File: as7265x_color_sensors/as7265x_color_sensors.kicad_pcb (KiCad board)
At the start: 2 copper layers, 37 parts, among them J1 Conn_01x06_Male, J2 RJ12, J3 RJ12, U1 AS72652, U2 AS72653, U3 AS72651, U4 AT25SF041

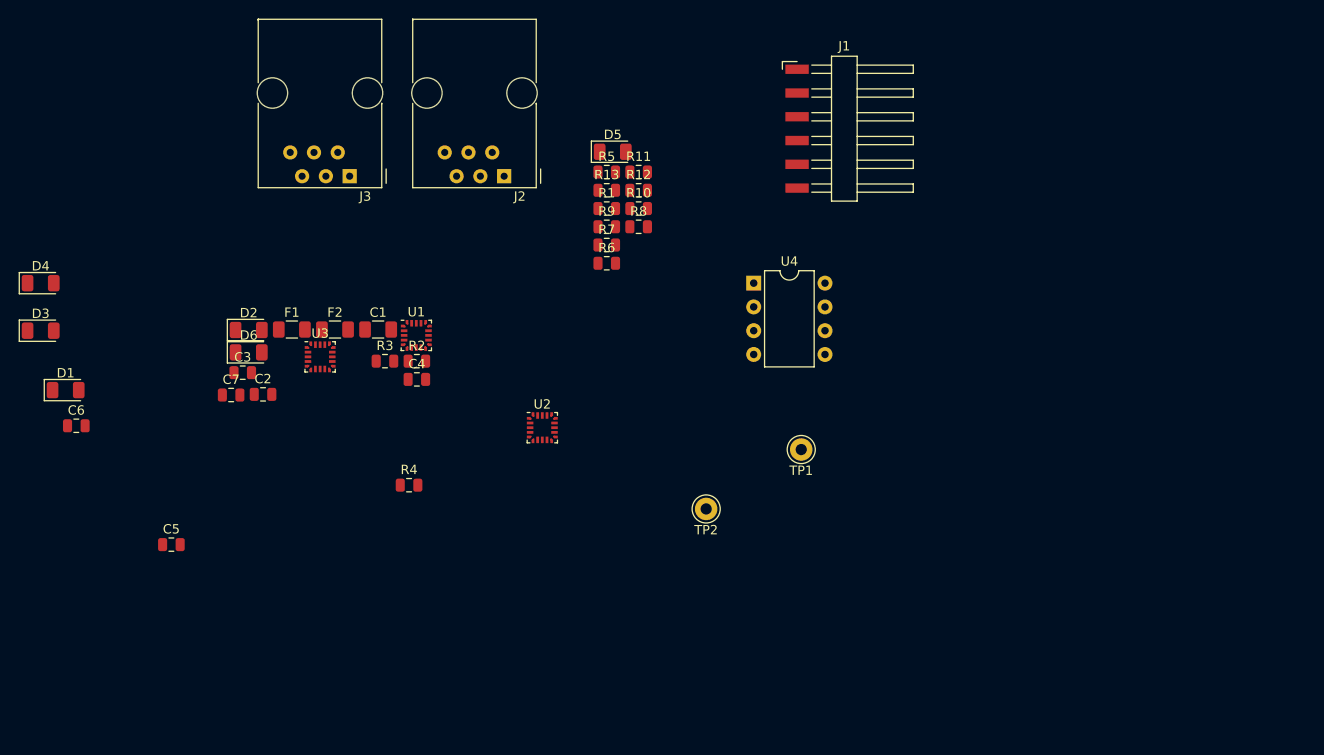
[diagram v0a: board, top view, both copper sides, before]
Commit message: chip footprints fixed, started layout
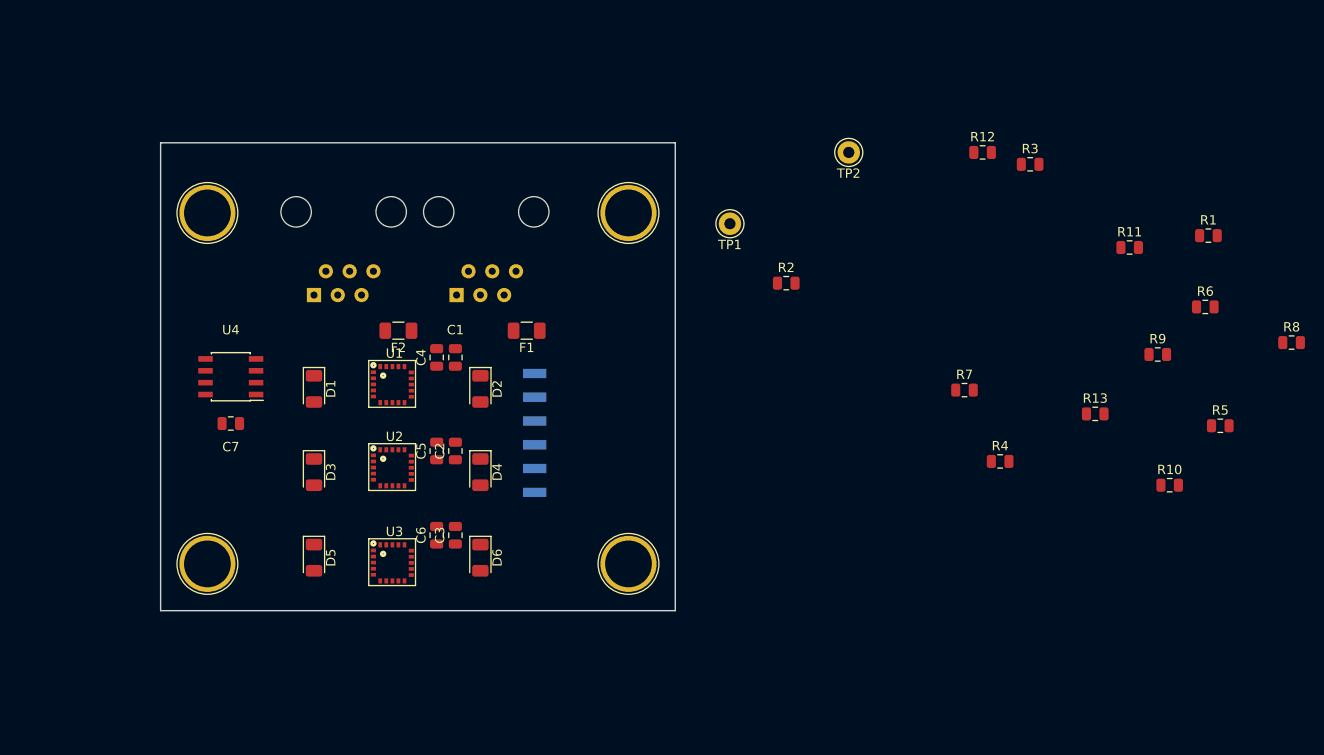
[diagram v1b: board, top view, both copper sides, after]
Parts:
- added REF**: TestPoint_Plated_Hole_D5.0mm, TestPoint:TestPoint_Plated_Hole_D5.0mm, F.Cu at (33.1, 40.8)
- added REF**: TestPoint_Plated_Hole_D5.0mm, TestPoint:TestPoint_Plated_Hole_D5.0mm, F.Cu at (78.1, 40.8)
- added REF**: TestPoint_Plated_Hole_D5.0mm, TestPoint:TestPoint_Plated_Hole_D5.0mm, F.Cu at (78.1, 78.3)
- added REF**: TestPoint_Plated_Hole_D5.0mm, TestPoint:TestPoint_Plated_Hole_D5.0mm, F.Cu at (33.1, 78.3)
- C1: footprint Capacitor_SMD:C_1206_3216Metric -> Capacitor_SMD:C_0805_2012Metric
- J1, J2, J3: moved to B.Cu
- U1: value AS72652 -> AS72651; footprint Package_DFN_QFN:ST_UFQFPN-20_3x3mm_P0.5mm -> MRV_SMD_Packages:LGA-20_4.5mm_4.7mm_2.5mm
- U2: value AS72653 -> AS72652; footprint Package_DFN_QFN:ST_UFQFPN-20_3x3mm_P0.5mm -> MRV_SMD_Packages:LGA-20_4.5mm_4.7mm_2.5mm
- U3: value AS72651 -> AS72653; footprint Package_DFN_QFN:ST_UFQFPN-20_3x3mm_P0.5mm -> MRV_SMD_Packages:LGA-20_4.5mm_4.7mm_2.5mm
- U4: footprint Package_DIP:DIP-8_W7.62mm -> Package_SO:SOIC-8_3.9x4.9mm_P1.27mm
- moved R3 72.1 mm to (121.0, 35.6)
- moved R5 71.0 mm to (141.3, 63.5)
- moved R8 70.9 mm to (148.9, 54.6)
- moved R1 64.4 mm to (140.0, 43.2)
- moved R6 64.1 mm to (139.7, 50.8)
- moved R10 64.0 mm to (135.9, 69.8)
- moved R4 63.2 mm to (117.8, 67.3)
- moved R9 60.4 mm to (134.6, 55.9)
- moved R13 57.4 mm to (127.9, 62.2)
- moved U4 56.8 mm to (35.6, 58.3), turned to 180 degrees
- moved D5 53.9 mm to (44.5, 77.6), turned to 270 degrees
- moved R11 53.1 mm to (131.6, 44.5)
- moved D4 51.1 mm to (62.2, 68.5), turned to 270 degrees
- moved J1 42.9 mm to (73.6, 64.3)
- moved R7 41.3 mm to (114.0, 59.7)
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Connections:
- U1 pad 11: Net-(U1-Pad11) -> /RXI
- U1 pad 12: Net-(U1-Pad12) -> /TXO
- U1 pad 13: Net-(U1-Pad13) -> /~INT
- U1 pad 15: /LED4 -> /LED2
- U1 pad 18: /LED3 -> /LED1
- U1 pad 5: Net-(R11-Pad2) -> Net-(U1-Pad5)
- U1 pad 7: Net-(R13-Pad2) -> Net-(U1-Pad7)
- U1 pad 8: Net-(U1-Pad8) -> Net-(R8-Pad1)
- U2 pad 15: /LED6 -> /LED4
- U2 pad 18: /LED5 -> /LED3
- U2 pad 5: Net-(R10-Pad2) -> Net-(R11-Pad2)
- U2 pad 7: Net-(R12-Pad2) -> Net-(R13-Pad2)
- U3 pad 11: /RXI -> Net-(U3-Pad11)
- U3 pad 12: /TXO -> Net-(U3-Pad12)
- U3 pad 13: /~INT -> Net-(U3-Pad13)
- U3 pad 15: /LED2 -> /LED6
- U3 pad 18: /LED1 -> /LED5
- U3 pad 5: Net-(U3-Pad5) -> Net-(R10-Pad2)
- U3 pad 7: Net-(U3-Pad7) -> Net-(R12-Pad2)
- U3 pad 8: Net-(R8-Pad1) -> Net-(U3-Pad8)
- U4 pad 1: Net-(U3-Pad6) -> Net-(U1-Pad6)
- U4 pad 2: Net-(U3-Pad5) -> Net-(U1-Pad5)
- U4 pad 5: Net-(U3-Pad4) -> Net-(U1-Pad4)
- U4 pad 6: Net-(U3-Pad3) -> Net-(U1-Pad3)
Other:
- board outline added: 55 x 50 mm

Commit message: adding TVS diode arrays
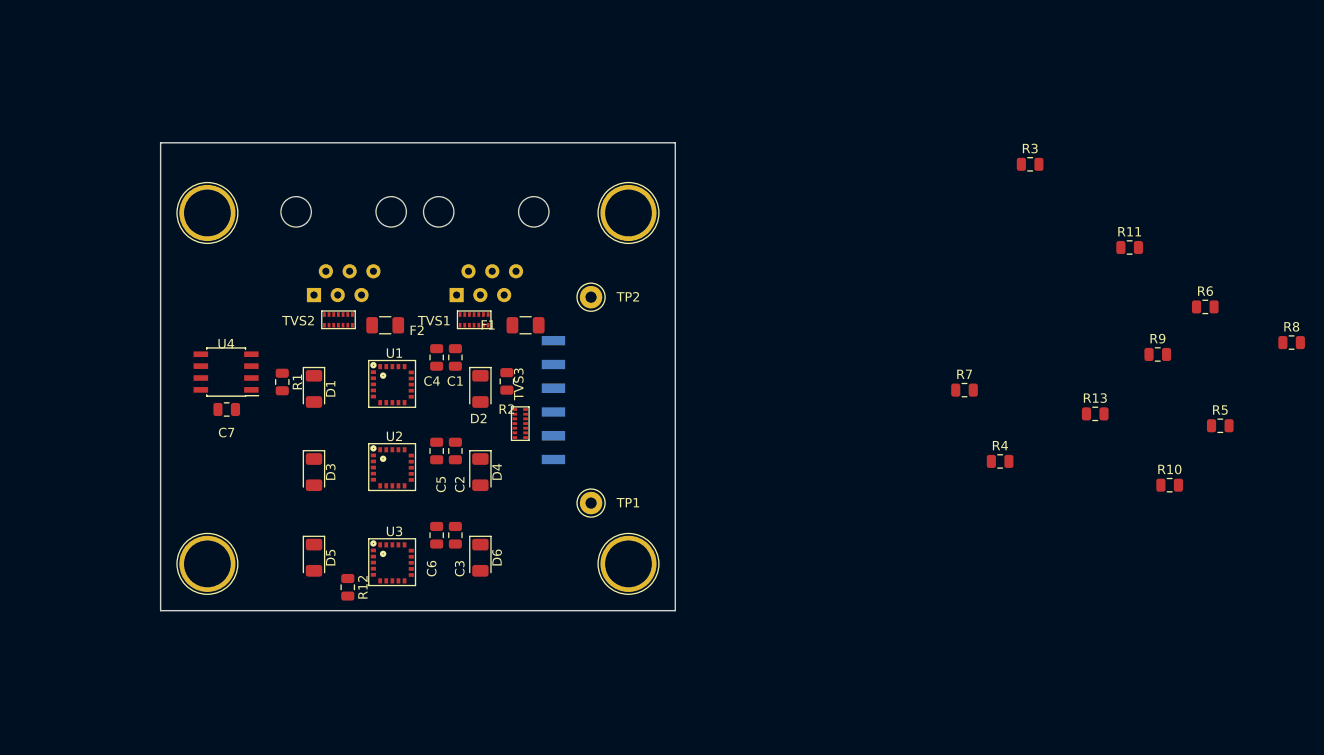
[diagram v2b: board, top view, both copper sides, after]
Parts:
- added TVS1: SP3012-06UTG, MRV_SMD_Packages:uDFN-14_3.5x1.35x0.5mm, F.Cu at (60.1, 52.8)
- added TVS2: SP3012-06UTG, MRV_SMD_Packages:uDFN-14_3.5x1.35x0.5mm, F.Cu at (45.6, 52.8)
- added TVS3: SP3012-06UTG, MRV_SMD_Packages:uDFN-14_3.5x1.35x0.5mm, F.Cu at (65.9, 61.8)
- moved R1 100.2 mm to (41.1, 58.8), turned to 270 degrees
- moved R12 82.2 mm to (48.1, 80.8), turned to 270 degrees
- moved TP1 33.3 mm to (74.1, 71.8)
- moved R2 31.6 mm to (65.1, 58.8), turned to 90 degrees
- moved TP2 31.6 mm to (74.1, 49.8)
- moved J1 4.03 mm to (75.6, 60.8)
- moved C7 1.56 mm to (35.1, 61.8)
- moved F2 1.52 mm to (52.1, 52.8), turned to 0 degrees
- moved U4 0.71 mm to (35.1, 57.8)
- moved F1 0.59 mm to (67.1, 52.8)

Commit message: added test points, more layout progress
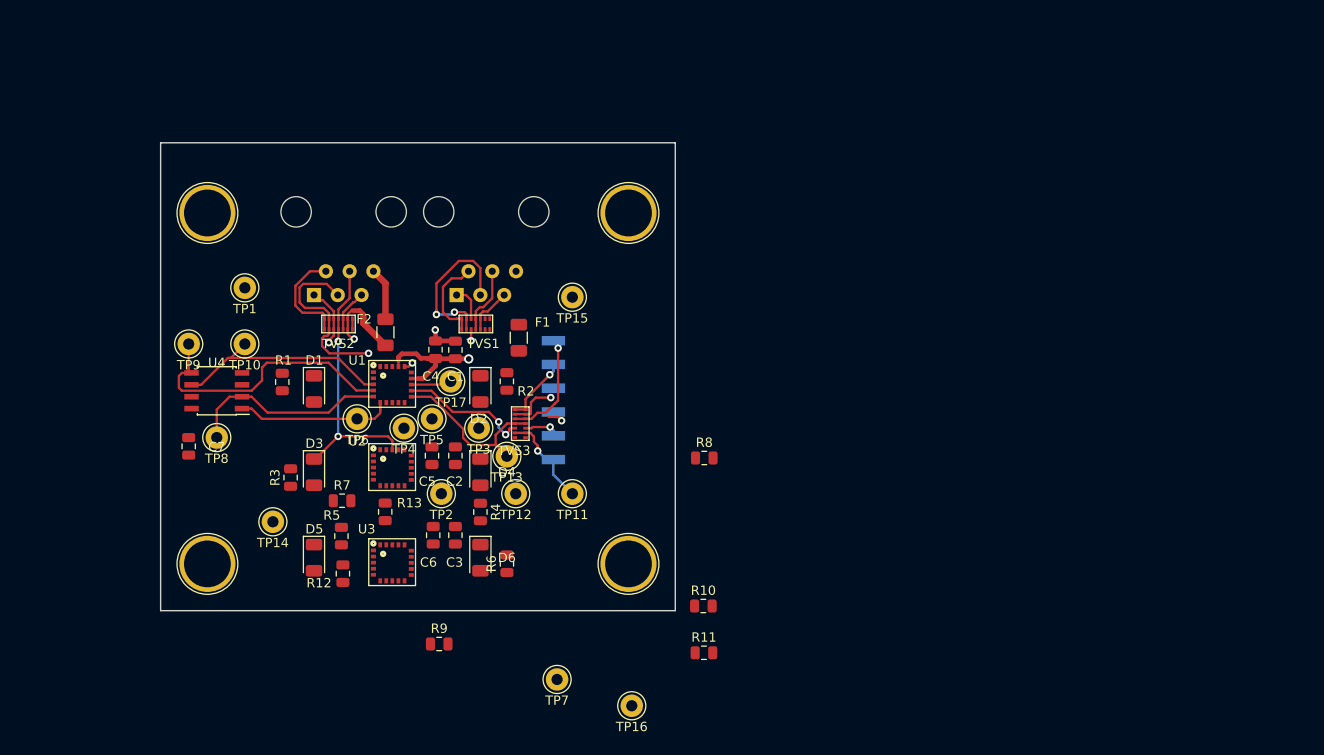
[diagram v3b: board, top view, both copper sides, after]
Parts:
- added TP10: TestPoint, Connector_Pin:Pin_D1.0mm_L10.0mm_LooseFit, F.Cu at (37.1, 54.8)
- added TP11: TestPoint, Connector_Pin:Pin_D1.0mm_L10.0mm_LooseFit, F.Cu at (72.1, 70.8)
- added TP12: TestPoint, Connector_Pin:Pin_D1.0mm_L10.0mm_LooseFit, F.Cu at (66.0, 70.8)
- added TP13: TestPoint, Connector_Pin:Pin_D1.0mm_L10.0mm_LooseFit, F.Cu at (65.1, 66.8)
- added TP14: TestPoint, Connector_Pin:Pin_D1.0mm_L10.0mm_LooseFit, F.Cu at (40.1, 73.8)
- added TP15: TestPoint, Connector_Pin:Pin_D1.0mm_L10.0mm_LooseFit, F.Cu at (72.1, 49.8)
- added TP16: TestPoint, Connector_Pin:Pin_D1.0mm_L10.0mm_LooseFit, F.Cu at (78.4, 93.4)
- added TP17: TestPoint, Connector_Pin:Pin_D1.0mm_L10.0mm_LooseFit, F.Cu at (59.1, 58.8)
- added TP3: TestPoint, Connector_Pin:Pin_D1.0mm_L10.0mm_LooseFit, F.Cu at (62.1, 63.8)
- added TP4: TestPoint, Connector_Pin:Pin_D1.0mm_L10.0mm_LooseFit, F.Cu at (54.1, 63.8)
- added TP5: TestPoint, Connector_Pin:Pin_D1.0mm_L10.0mm_LooseFit, F.Cu at (57.1, 62.8)
- added TP6: TestPoint, Connector_Pin:Pin_D1.0mm_L10.0mm_LooseFit, F.Cu at (49.1, 62.8)
- added TP7: TestPoint, Connector_Pin:Pin_D1.0mm_L10.0mm_LooseFit, F.Cu at (70.4, 90.6)
- added TP8: TestPoint, Connector_Pin:Pin_D1.0mm_L10.0mm_LooseFit, F.Cu at (34.1, 64.8)
- added TP9: TestPoint, Connector_Pin:Pin_D1.0mm_L10.0mm_LooseFit, F.Cu at (31.1, 54.8)
- moved R5 94.7 mm to (47.4, 75.3), turned to 90 degrees
- moved R3 85.8 mm to (42.0, 69.0), turned to 90 degrees
- moved R9 82.8 mm to (57.8, 86.8)
- moved R6 79.5 mm to (65.1, 78.2), turned to 90 degrees
- moved R13 76.6 mm to (52.1, 72.7), turned to 90 degrees
- moved R7 67.6 mm to (47.5, 71.5)
- moved R8 64.0 mm to (86.2, 66.9)
- moved R11 62.8 mm to (86.1, 87.8)
- moved R4 55.8 mm to (62.2, 72.7), turned to 270 degrees
- moved R10 51.5 mm to (86.1, 82.8)
- moved TP1 43.6 mm to (37.1, 48.8)
- moved TP2 26.4 mm to (58.1, 70.8)
- moved C7 5.66 mm to (31.1, 65.7), turned to 270 degrees
- moved U4 2.24 mm to (34.1, 59.8)
- moved R12 1.54 mm to (47.5, 79.3)
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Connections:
- TP1 pad 1: /DTR -> +3V3
- TP2 pad 1: /CTS -> Net-(TP2-Pad1)
- U1 pad 10: Net-(U1-Pad10) -> Net-(TP2-Pad1)
- U2 pad 10: Net-(U1-Pad10) -> Net-(TP2-Pad1)
- U3 pad 10: Net-(U1-Pad10) -> Net-(TP2-Pad1)
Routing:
- net Net-(TP9-Pad1): track 0.00 -> 30.1 mm
- net /LED3: track 0.00 -> 28.7 mm, vias 0 -> 2
- net /RXI: track 0.00 -> 28.3 mm, vias 0 -> 1
- net GND: track 0.00 -> 27.7 mm, vias 0 -> 5
- net +3V3: track 0.00 -> 27.4 mm, vias 0 -> 3
- net Net-(TP10-Pad1): track 0.00 -> 24.2 mm
- net /TXO: track 0.00 -> 22.5 mm, vias 0 -> 3
- net Net-(TP8-Pad1): track 0.00 -> 21.7 mm
- net /LED2: track 0.00 -> 19.2 mm, vias 0 -> 1
- net /LED6: track 0.00 -> 17.4 mm, vias 0 -> 2
- net Net-(TP6-Pad1): track 0.00 -> 17.1 mm
- net /LED1: track 0.00 -> 11.2 mm
- net /DTR: track 0.00 -> 10.5 mm, vias 0 -> 1
- net /LED5: track 0.00 -> 9.58 mm
- net /CTS: track 0.00 -> 7.19 mm, vias 0 -> 1
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
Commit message: worked on layout
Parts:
- R8, R9: moved to B.Cu
- moved R11 44.1 mm to (46.8, 67.8), turned to 90 degrees
- moved R10 36.9 mm to (49.3, 79.2), turned to 90 degrees
- moved R8 30.9 mm to (56.4, 58.8), turned to 90 degrees
- moved R9 28.4 mm to (62.0, 58.8), turned to 270 degrees
- moved TP7 13.1 mm to (57.7, 87.6)
- moved TP16 7.69 mm to (73.0, 88.0)
- moved C5 1.63 mm to (58.3, 65.7), turned to 0 degrees
- moved C2 1.62 mm to (58.3, 67.8), turned to 0 degrees
- moved TP4 1.50 mm to (52.6, 63.5)
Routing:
- net /LED5: track 9.58 -> 76.3 mm, vias 0 -> 3
- net /LED6: track 17.4 -> 73.6 mm, vias 2 -> 4
- net Net-(TP3-Pad1): track 0.00 -> 55.4 mm, vias 0 -> 3
- net +3V3: track 27.4 -> 79.6 mm, vias 3 -> 17
- net Net-(TP2-Pad1): track 0.00 -> 30.9 mm, vias 0 -> 2
- net Net-(R7-Pad2): track 0.00 -> 29.5 mm, vias 0 -> 2
- net /RXI: track 28.3 -> 51.7 mm, vias 1 -> 2
- net /LED1: track 11.2 -> 30.3 mm, vias 0 -> 3
- net /LED2: track 19.2 -> 36.2 mm, vias 1 -> 3
- net GND: track 27.7 -> 43.4 mm, vias 5 -> 15
- net Net-(R8-Pad1): track 0.00 -> 14.8 mm
- net /LED4: track 4.84 -> 16.3 mm, vias 0 -> 3
- net /TXO: track 22.5 -> 31.9 mm, vias 3 -> 4
- net /CTS: track 7.19 -> 16.5 mm
- net Net-(R12-Pad2): track 0.00 -> 6.42 mm
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- added copper zone on In2.Cu, net +3V3
- added copper zone on In1.Cu, net GND
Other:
- copper layers 2 -> 4

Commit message: layout looks just about done
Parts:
- removed TP16, TP7: TestPoint, Connector_Pin:Pin_D1.0mm_L10.0mm_LooseFit
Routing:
- net /LED4: track 16.3 -> 31.2 mm
- net /TXO: track 31.9 -> 45.6 mm, vias 4 -> 5
- net +3V3: track 79.6 -> 87.6 mm, vias 17 -> 18
- net Net-(D1-Pad2): track 0.31 -> 4.66 mm
- net Net-(D2-Pad2): track 0.00 -> 3.35 mm
- net Net-(TVS3-Pad14): track 0.00 -> 1.15 mm
- net GND: track 43.4 -> 44.5 mm
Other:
- board text added: "8/11/18"
- board text added: "AS7265X BREAKOUT"
- board text added: "Color Sensors"
- board text added: "Matt Valancy"

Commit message: added pic and gerbers
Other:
- board text added: "github.com/scubasonar"
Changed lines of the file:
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@@
   (general
     (thickness 1.6)
-    (drawings 14)
+    (drawings 15)
     (tracks 635)
     (zones 0)
@@
   (page A4)
   (layers
-    (0 F.Cu signal)
-    (1 In1.Cu power hide)
+    (0 F.Cu signal hide)
+    (1 In1.Cu power)
     (2 In2.Cu power hide)
     (31 B.Cu signal)
@@
     (34 B.Paste user hide)
     (35 F.Paste user hide)
-    (36 B.SilkS user hide)
+    (36 B.SilkS user)
     (37 F.SilkS user)
     (38 B.Mask user hide)
@@
     (visible_elements 7FFFFFFF)
     (pcbplotparams
-      (layerselection 0x010fc_ffffffff)
+      (layerselection 0x010f0_ffffffff)
       (usegerberextensions false)
       (usegerberattributes false)
@@
       (outputformat 1)
       (mirror false)
-      (drillshape 1)
+      (drillshape 0)
       (scaleselection 1)
-      (outputdirectory ""))
+      (outputdirectory "gerbers/"))
   )
   (net 0 "")
@@
     (descr "RJ12 connector  https://cdn.amphenol-icc.com/media/wysiwyg/files/drawing/c-bmj-0082.pdf")
     (tags "RJ12 connector")
-    (fp_text reference J2 (at -1.67 2.16) (layer B.SilkS)
+    (fp_text reference J2 (at 5.92 2.25) (layer B.SilkS)
       (effects (font (size 1 1) (thickness 0.15)) (justify mirror))
     )
@@
     (descr "RJ12 connector  https://cdn.amphenol-icc.com/media/wysiwyg/files/drawing/c-bmj-0082.pdf")
     (tags "RJ12 connector")
-    (fp_text reference J3 (at -1.67 2.16) (layer B.SilkS)
+    (fp_text reference J3 (at 6.63 2.14) (layer B.SilkS)
       (effects (font (size 1 1) (thickness 0.15)) (justify mirror))
     )
@@
     (tags resistor)
     (attr smd)
-    (fp_text reference R8 (at 0 1.65 90) (layer B.SilkS)
+    (fp_text reference R8 (at -0.3675 -1.928 90) (layer B.SilkS)
       (effects (font (size 1 1) (thickness 0.15)) (justify mirror))
     )
@@
     (tags resistor)
     (attr smd)
-    (fp_text reference R9 (at 0 1.65 270) (layer B.SilkS)
+    (fp_text reference R9 (at 0.0775 -1.674 270) (layer B.SilkS)
       (effects (font (size 1 1) (thickness 0.15)) (justify mirror))
     )
@@
     )
   )
+  (gr_text github.com/scubasonar (at 80.32 58.54 90) (layer F.SilkS)
+    (effects (font (size 1.5 1.5) (thickness 0.3)))
+  )
   (gr_text "Color Sensors" (at 56.38 44.18) (layer F.SilkS)
     (effects (font (size 2 2) (thickness 0.3)))
   )
-  (gr_text "Matt Valancy" (at 80.74 58.63 90) (layer F.SilkS)
+  (gr_text "Matt Valancy" (at 77.22 58.66 90) (layer F.SilkS)
     (effects (font (size 2 2) (thickness 0.3)))
   )
-  (gr_text 8/11/18 (at 34.01 35.71) (layer F.SilkS)
+  (gr_text 8/11/18 (at 73.95 59.4 90) (layer F.SilkS)
     (effects (font (size 1.5 1.5) (thickness 0.3)))
   )
